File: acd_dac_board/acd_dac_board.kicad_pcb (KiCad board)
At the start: 2 copper layers, 85 x 64 mm, 4 parts, among them J1 Conn_02x10_Odd_Even, J2 Conn_02x10_Odd_Even, J3 Conn_02x10_Odd_Even, J4 Conn_02x25_Odd_Even

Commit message: update adc_dac board
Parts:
- added REF**: MountingHole_2.5mm, MountingHole:MountingHole_2.5mm, F.Cu at (117.5, 92.4)
- added REF**: MountingHole_2.5mm, MountingHole:MountingHole_2.5mm, F.Cu at (174.1, 126.7)
- added REF**: MountingHole_2.5mm, MountingHole:MountingHole_2.5mm, F.Cu at (154.1, 75.5)
- added REF**: MountingHole_2.5mm, MountingHole:MountingHole_2.5mm, F.Cu at (99.7, 75.7)
- added REF**: MountingHole_2.5mm, MountingHole:MountingHole_2.5mm, F.Cu at (99.2, 126.3)
- added REF**: MountingHole_2.5mm, MountingHole:MountingHole_2.5mm, F.Cu at (129.0, 75.7)
- added REF**: MountingHole_2.5mm, MountingHole:MountingHole_2.5mm, F.Cu at (163.7, 75.9)
- added REF**: MountingHole_2.5mm, MountingHole:MountingHole_2.5mm, F.Cu at (128.8, 88.4)
- added REF**: MountingHole_2.5mm, MountingHole:MountingHole_2.5mm, F.Cu at (154.3, 93.0)
- added REF**: MountingHole_2.5mm, MountingHole:MountingHole_2.5mm, F.Cu at (169.0, 113.4)
- added REF**: MountingHole_2.5mm, MountingHole:MountingHole_2.5mm, F.Cu at (117.2, 75.7)
- added REF**: MountingHole_2.5mm, MountingHole:MountingHole_2.5mm, F.Cu at (99.9, 113.3)
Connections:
- J1 pad 10: /D3 -> /B11
- J1 pad 11: /D6 -> /D11
- J1 pad 12: /D5 -> /D10
- J1 pad 13: /D8 -> /C9
- J1 pad 14: /D7 -> /D9
- J1 pad 15: /D10 -> /A10
- J1 pad 16: /D9 -> /B10
- J1 pad 17: /OTR -> /A9
- J1 pad 18: /D11 -> /B9
- J1 pad 5: /D0 -> /F14
- J1 pad 6: /CLK -> /E13
- J1 pad 7: /D2 -> /B12
- J1 pad 8: /D1 -> /A12
- J1 pad 9: /D4 -> /C11
- J2 pad 13: /B15 -> /B17
- J2 pad 14: /A15 -> /A17
- J2 pad 17: /B17 -> /B15
- J2 pad 18: /A17 -> /A15
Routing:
- net /D15: track 0.00 -> 51.8 mm
- net /E13: track 0.00 -> 49.1 mm
- net /E15: track 0.00 -> 47.6 mm
- net /A12: track 0.00 -> 45.5 mm
- net /C12: track 0.00 -> 45.2 mm
- net /F14: track 0.00 -> 44.5 mm
- net /G16: track 0.00 -> 44.0 mm
- net /E16: track 0.00 -> 43.0 mm
- net /B11: track 0.00 -> 41.9 mm
- net /D13: track 0.00 -> 41.6 mm
- net /B12: track 0.00 -> 40.9 mm
- net /A13: track 0.00 -> 40.6 mm
- net /H16: track 0.00 -> 40.4 mm
- net /F15: track 0.00 -> 39.5 mm
- net /D10: track 0.00 -> 38.4 mm
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
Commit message: update
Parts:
- removed the REF** at (117.5, 92.4)
- removed the REF** at (174.1, 126.7)
- removed the REF** at (154.1, 75.5)
- removed the REF** at (99.2, 126.3)
- removed the REF** at (129.0, 75.7)
- removed the REF** at (163.7, 75.9)
- removed the REF** at (128.8, 88.4)
- removed the REF** at (154.3, 93.0)
- removed the REF** at (169.0, 113.4)
- removed the REF** at (117.2, 75.7)
- removed the REF** at (99.9, 113.3)
- added REF**: MountingHole_2.5mm, MountingHole:MountingHole_2.5mm, B.Cu at (160.3, 90.9)
- added REF**: MountingHole_2.5mm, MountingHole:MountingHole_2.5mm, B.Cu at (162.4, 75.7)
- added REF**: MountingHole_2.5mm, MountingHole:MountingHole_2.5mm, B.Cu at (124.3, 97.8)
- added REF**: MountingHole_2.5mm, MountingHole:MountingHole_2.5mm, B.Cu at (174.7, 125.5)
- added REF**: MountingHole_2.5mm, MountingHole:MountingHole_2.5mm, B.Cu at (97.9, 124.6)
- added REF**: MountingHole_2.5mm, MountingHole:MountingHole_2.5mm, B.Cu at (130.8, 75.3)
- added REF**: MountingHole_2.5mm, MountingHole:MountingHole_2.5mm, B.Cu at (99.4, 114.3)
- REF**: moved to B.Cu
- turned REF** to 180 degrees

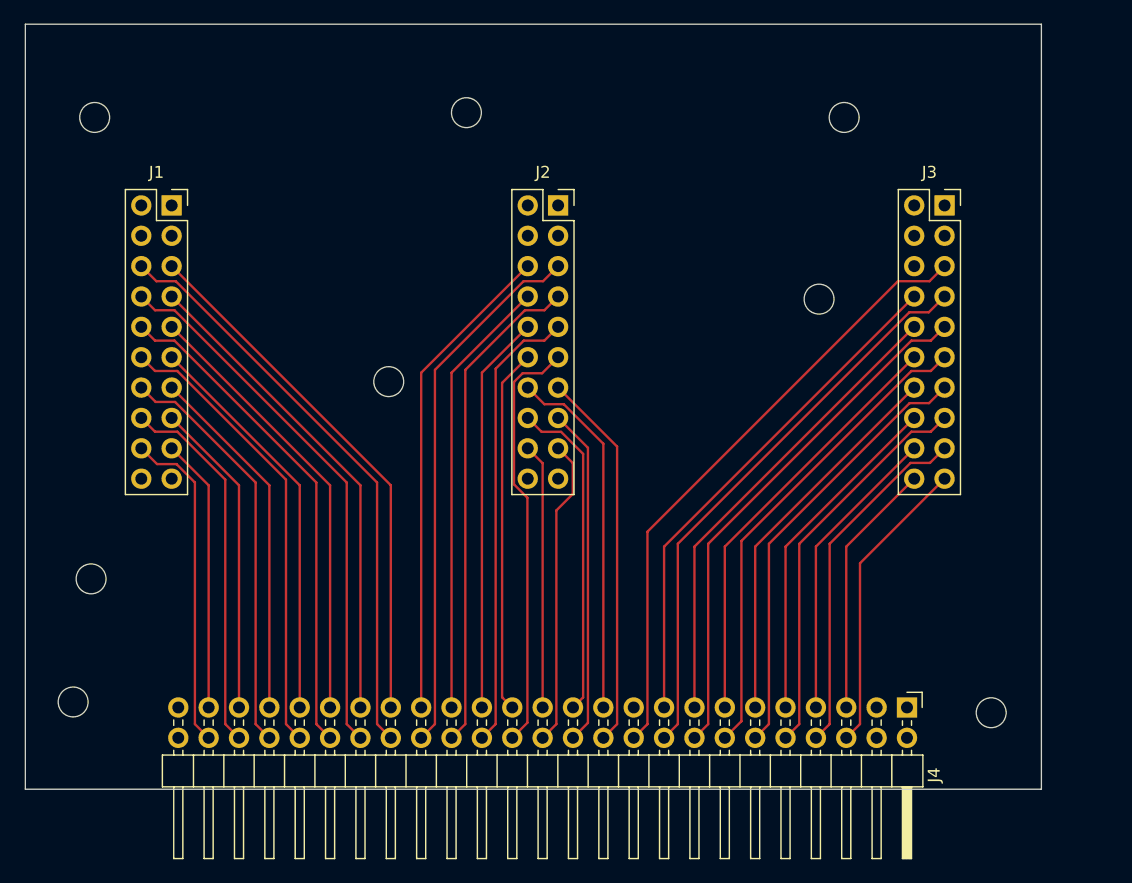
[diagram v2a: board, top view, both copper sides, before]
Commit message: add initial version of holder
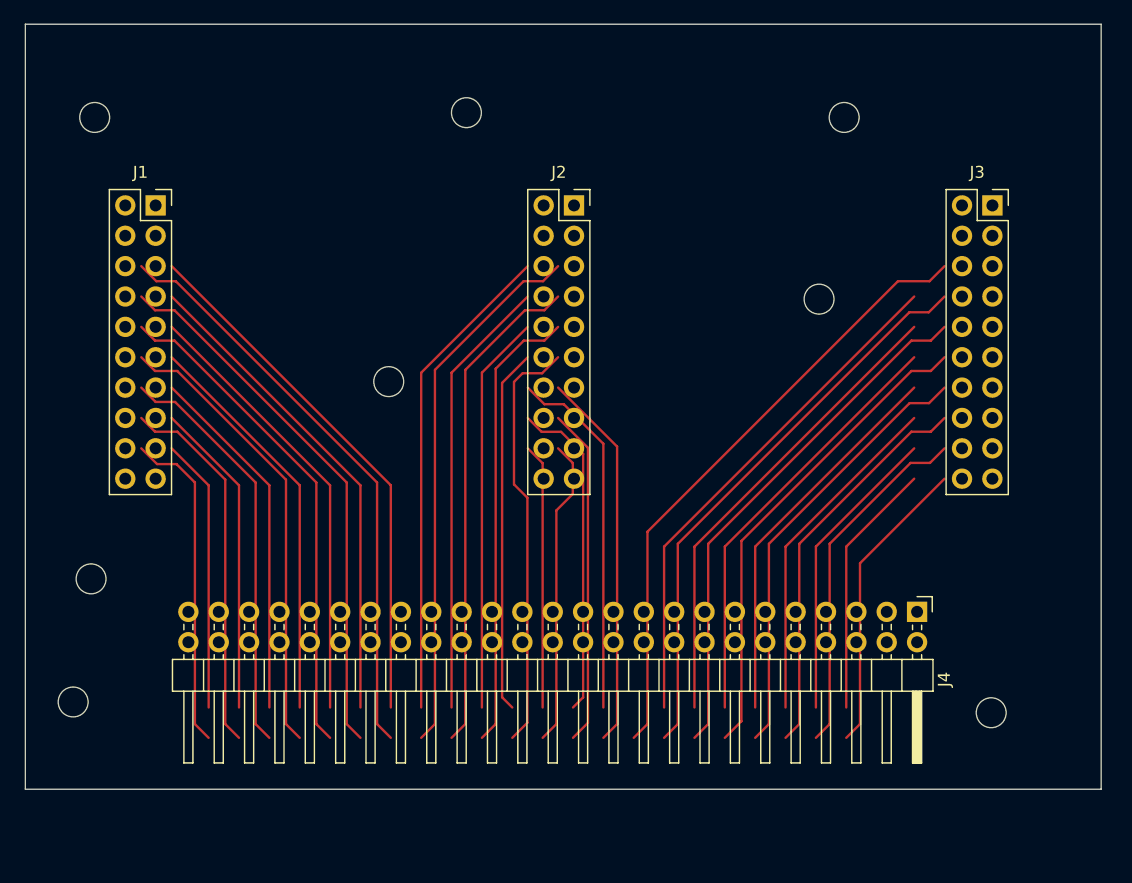
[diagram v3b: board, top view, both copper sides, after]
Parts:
- moved J4 8.04 mm to (168.5, 117.1)
- moved J3 4.00 mm to (174.8, 83.1)
- moved J1 1.34 mm to (104.8, 83.1)
- moved J2 1.33 mm to (139.8, 83.1)
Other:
- board size 85 x 64 mm -> 90 x 64 mm
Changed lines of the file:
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@@
 	(footprint "Connector_PinHeader_2.54mm:PinHeader_2x25_P2.54mm_Horizontal"
 		(layer "F.Cu")
-		(at 167.655 125.06 -90)
+		(at 168.5 117.06 -90)
 		(descr "Through hole angled pin header, 2x25, 2.54mm pitch, 6mm pin length, double rows")
 		(tags "Through hole angled pin header THT 2x25 2.54mm double row")
@@
 	(footprint "Connector_PinSocket_2.54mm:PinSocket_2x10_P2.54mm_Vertical"
 		(layer "F.Cu")
-		(at 170.8 83.06)
+		(at 174.8 83.06)
 		(descr "Through hole straight socket strip, 2x10, 2.54mm pitch, double cols (from Kicad 4.0.7), script generated")
 		(tags "Through hole socket strip THT 2x10 2.54mm double row")
@@
 	(footprint "Connector_PinSocket_2.54mm:PinSocket_2x10_P2.54mm_Vertical"
 		(layer "F.Cu")
-		(at 106.14 83.06)
+		(at 104.8 83.06)
 		(descr "Through hole straight socket strip, 2x10, 2.54mm pitch, double cols (from Kicad 4.0.7), script generated")
 		(tags "Through hole socket strip THT 2x10 2.54mm double row")
@@
 	(footprint "Connector_PinSocket_2.54mm:PinSocket_2x10_P2.54mm_Vertical"
 		(layer "F.Cu")
-		(at 138.47 83.06)
+		(at 139.8 83.06)
 		(descr "Through hole straight socket strip, 2x10, 2.54mm pitch, double cols (from Kicad 4.0.7), script generated")
 		(tags "Through hole socket strip THT 2x10 2.54mm double row")
@@
 	(gr_rect
 		(start 93.9 67.9)
-		(end 178.9 131.9)
+		(end 183.9 131.9)
 		(stroke
 			(width 0.05)

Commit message: route adc_dac board (fix errors). Finish first version of holder
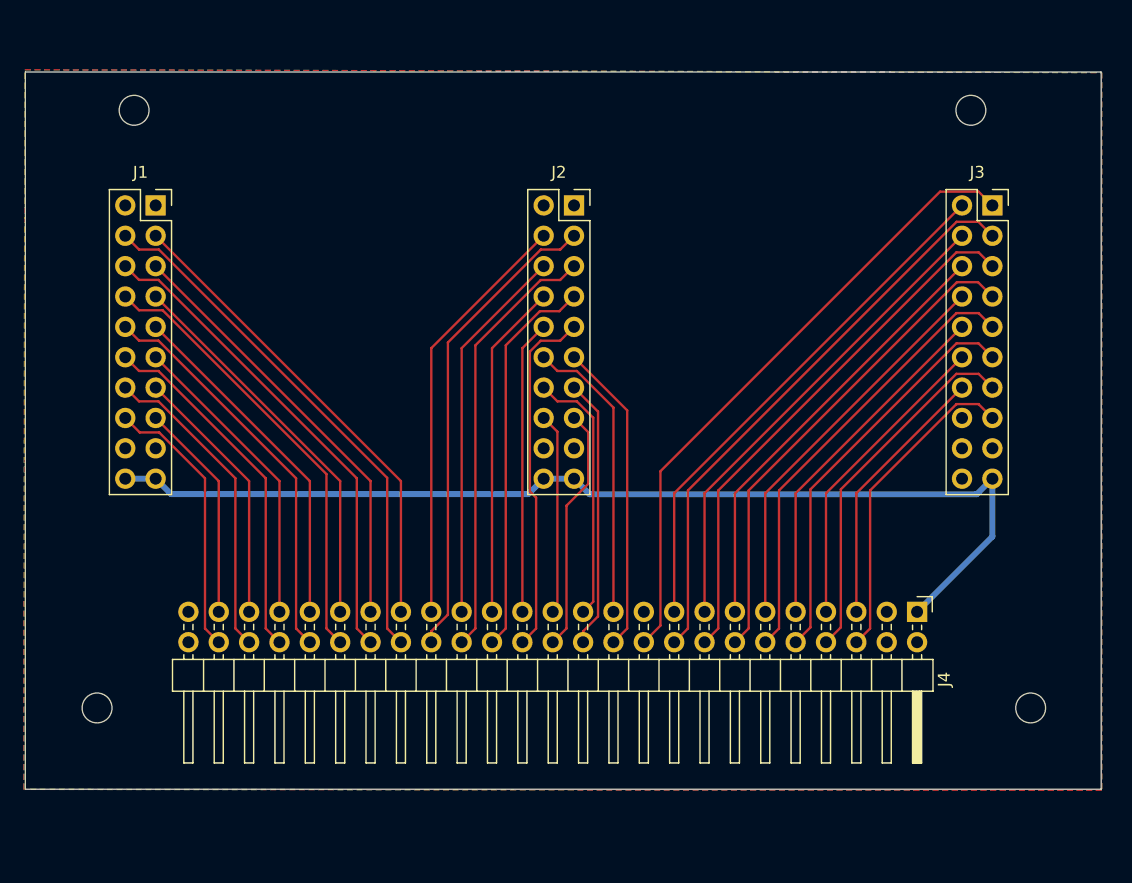
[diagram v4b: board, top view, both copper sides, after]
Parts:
- removed the REF** at (160.3, 90.9)
- removed the REF** at (124.3, 97.8)
- removed the REF** at (130.8, 75.3)
- removed the REF** at (99.4, 114.3)
- moved REF** 10.6 mm to (173.0, 75.1)
- moved REF** 3.35 mm to (103.0, 75.1)
- moved REF** 3.32 mm to (178.0, 125.1)
- moved REF** 2.06 mm to (99.9, 125.1)
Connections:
- J1 pad 1: +5V -> GND
- J1 pad 10: /B11 -> /D10
- J1 pad 11: /D11 -> /C9
- J1 pad 12: /D10 -> /D9
- J1 pad 13: /C9 -> /A10
- J1 pad 14: /D9 -> /B10
- J1 pad 15: /A10 -> /A9
- J1 pad 16: /B10 -> /B9
- J1 pad 17: /A9 -> GND
- J1 pad 18: /B9 -> GND
- J1 pad 19: GND -> +5V
- J1 pad 2: +5V -> GND
- J1 pad 20: GND -> +5V
- J1 pad 3: GND -> /F14
- J1 pad 4: GND -> /E13
- J1 pad 5: /F14 -> /B12
- J1 pad 6: /E13 -> /A12
- J1 pad 7: /B12 -> /C11
- J1 pad 8: /A12 -> /B11
- J1 pad 9: /C11 -> /D11
- J2 pad 1: +5V -> GND
- J2 pad 10: /C14 -> /A14
- J2 pad 11: /B14 -> /B17
- J2 pad 12: /A14 -> /A17
- J2 pad 13: /B17 -> /B16
- J2 pad 14: /A17 -> /C16
- J2 pad 15: /B16 -> /B15
- J2 pad 16: /C16 -> /A15
- J2 pad 17: /B15 -> GND
- J2 pad 18: /A15 -> GND
- J2 pad 19: GND -> +5V
- J2 pad 2: +5V -> GND
- J2 pad 20: GND -> +5V
- J2 pad 3: GND -> /C12
- J2 pad 4: GND -> /A13
- J2 pad 5: /C12 -> /D13
- J2 pad 6: /A13 -> /C13
- J2 pad 7: /D13 -> /D14
- J2 pad 8: /C13 -> /C14
- J2 pad 9: /D14 -> /B14
- J3 pad 1: GND -> /D15
- J3 pad 10: /F15 -> /D18
- J3 pad 11: /H16 -> /E17
- J3 pad 12: /G15 -> /E18
- J3 pad 13: /C18 -> /F17
- J3 pad 14: /C17 -> /F18
- J3 pad 15: /E17 -> /G17
- J3 pad 16: /D18 -> GND
- J3 pad 17: /F17 -> GND
- J3 pad 18: /E18 -> GND
- J3 pad 19: /G17 -> +5V
- J3 pad 2: +5V -> /E16
- J3 pad 20: /F18 -> GND
- J3 pad 3: GND -> /E15
- J3 pad 4: GND -> /F15
- J3 pad 5: /D15 -> /G16
- J3 pad 6: GND -> /G15
- J3 pad 7: /E15 -> /H16
- J3 pad 8: /E16 -> /C17
- J3 pad 9: /G16 -> /C18
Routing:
- net +5V: track 0.00 -> 88.4 mm
- net /A14: track 30.5 -> 24.6 mm
- net /B14: track 35.3 -> 29.6 mm
- net /B17: track 31.8 -> 26.2 mm
- net /B16: track 28.3 -> 22.7 mm
- net /A17: track 30.3 -> 24.7 mm
- net /C16: track 27.4 -> 21.8 mm
- net /A15: track 22.2 -> 16.9 mm
- net /D14: track 38.0 -> 32.7 mm
- net /B15: track 25.8 -> 20.5 mm
- net /C14: track 33.4 -> 28.2 mm
- net /C13: track 37.0 -> 31.8 mm
- net /A13: track 40.6 -> 35.4 mm
- net /D13: track 41.6 -> 36.3 mm
- net /C12: track 45.2 -> 39.9 mm
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- added copper zone on B.Cu, net GND
- added copper zone on F.Cu, net GND
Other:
- board size 90 x 64 mm -> 90 x 60 mm

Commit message: fix adc board pinout
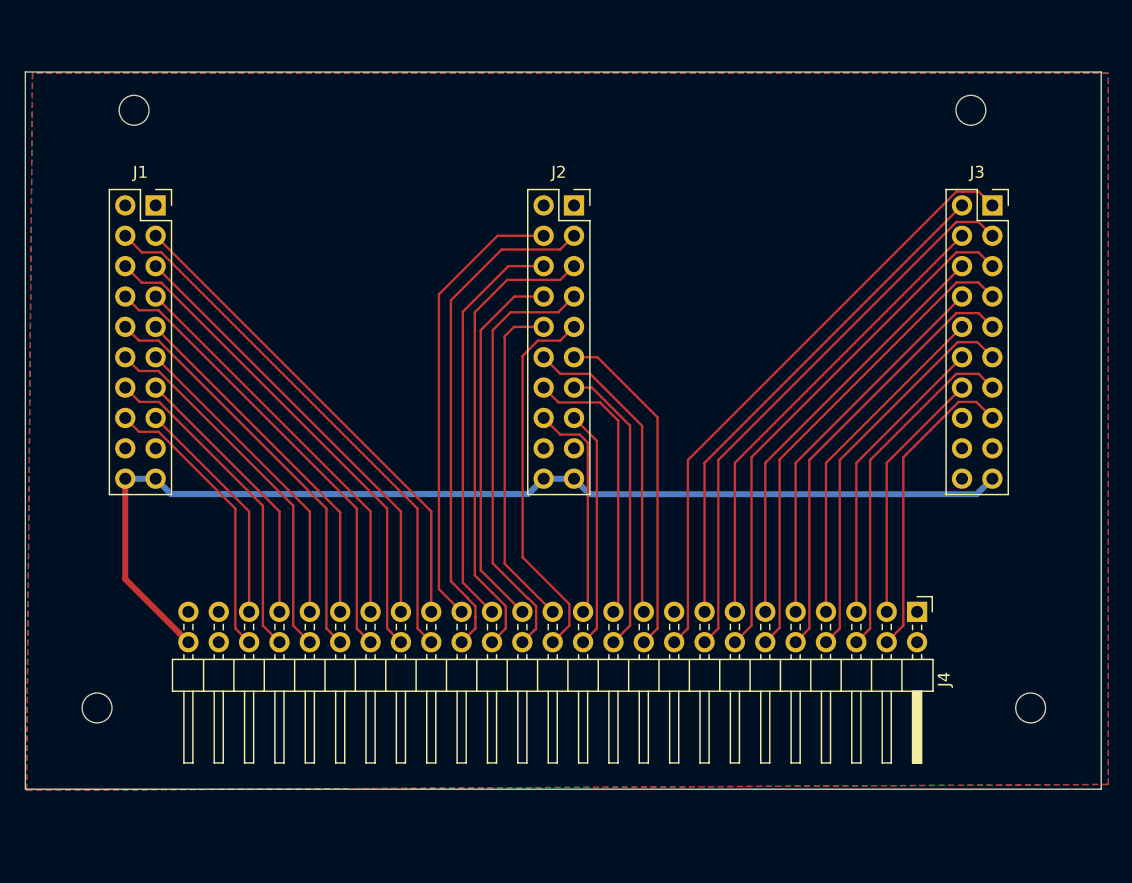
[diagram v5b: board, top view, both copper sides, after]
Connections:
- J4 pad 1: +5V -> GND
- J4 pad 10: /E17 -> /C18
- J4 pad 11: /C17 -> /G15
- J4 pad 12: /C18 -> /H16
- J4 pad 13: /G15 -> /F15
- J4 pad 14: /H16 -> /G16
- J4 pad 15: /F15 -> /E16
- J4 pad 16: /G16 -> /E15
- J4 pad 17: /E16 -> /D16
- J4 pad 18: /E15 -> /D15
- J4 pad 19: /D16 -> /A17
- J4 pad 2: +3.3V -> GND
- J4 pad 20: /D15 -> /B17
- J4 pad 21: /A17 -> /C16
- J4 pad 22: /B17 -> /B16
- J4 pad 23: /C16 -> /A15
- J4 pad 24: /B16 -> /B15
- J4 pad 25: /A15 -> /A14
- J4 pad 26: /B15 -> /B14
- J4 pad 27: /A14 -> /C14
- J4 pad 28: /B14 -> /D14
- J4 pad 29: /C14 -> /C13
- J4 pad 3: GND -> /F18
- J4 pad 30: /D14 -> /D13
- J4 pad 31: /C13 -> /A13
- J4 pad 32: /D13 -> /C12
- J4 pad 33: /A13 -> /F14
- J4 pad 34: /C12 -> /E13
- J4 pad 35: /F14 -> /B12
- J4 pad 36: /E13 -> /A12
- J4 pad 37: /B12 -> /C11
- J4 pad 38: /A12 -> /B11
- J4 pad 39: /C11 -> /D11
- J4 pad 4: GND -> /G17
- J4 pad 40: /B11 -> /D10
- J4 pad 41: /D11 -> /C9
- J4 pad 42: /D10 -> /D9
- J4 pad 43: /C9 -> /A10
- J4 pad 44: /D9 -> /B10
- J4 pad 45: /A10 -> /A9
- J4 pad 46: /B10 -> /B9
- J4 pad 47: /A9 -> GND
- J4 pad 48: /B9 -> GND
- J4 pad 49: GND -> +3.3V
- J4 pad 5: /F18 -> /E18
- J4 pad 50: GND -> +5V
- J4 pad 6: /G17 -> /F17
- J4 pad 7: /E18 -> /D18
- J4 pad 8: /F17 -> /E17
- J4 pad 9: /D18 -> /C17
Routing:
- net /A14: track 24.6 -> 28.3 mm
- net /D14: track 32.7 -> 36.1 mm
- net /C14: track 28.2 -> 31.4 mm
- net /A13: track 35.4 -> 38.1 mm
- net /D13: track 36.3 -> 39.1 mm
- net /C13: track 31.8 -> 34.5 mm
- net /C12: track 39.9 -> 42.6 mm
- net /B17: track 26.2 -> 28.4 mm
- net +5V: track 88.4 -> 90.6 mm
- net /B16: track 22.7 -> 24.7 mm
- net /A15: track 16.9 -> 18.9 mm
- net /B14: track 29.6 -> 31.4 mm
- net /D15: track 52.8 -> 51.0 mm
- net /C16: track 21.8 -> 23.5 mm
- net /A17: track 24.7 -> 26.2 mm
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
